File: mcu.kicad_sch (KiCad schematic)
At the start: 29 parts, among them U1 NRF52840-QIAA-R, Y1 32.768 kHz, Y2 32 MHz

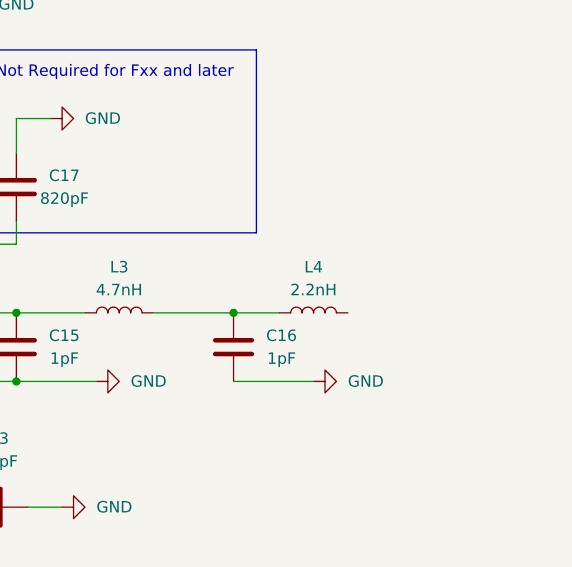
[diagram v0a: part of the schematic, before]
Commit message: Added 0 Ohm resistor before antenna for later VNA tuning
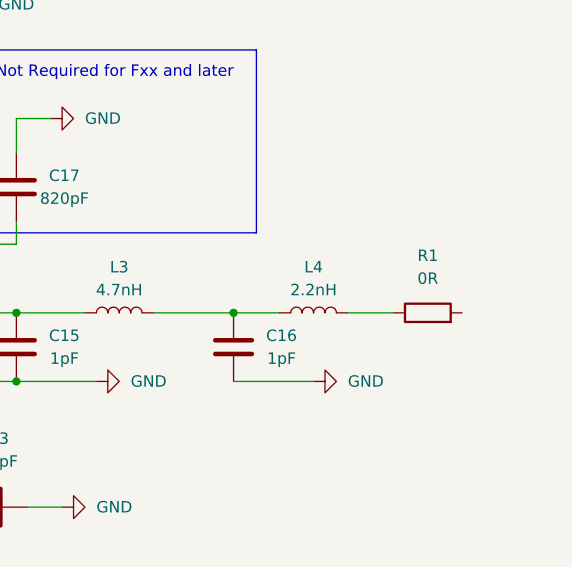
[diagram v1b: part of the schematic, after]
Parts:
- added R1: 0R, symbol Device:R
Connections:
- net at L4.2: now also R1.1
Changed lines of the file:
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@@
+	(wire
+		(pts
+			(xy 255.27 120.65) (xy 260.35 120.65)
+		)
+		(stroke
+			(width 0)
+			(type default)
+		)
+	)
 	(wire
 		(pts
@@
 					(unit 1)
 				)
+			)
+		)
+	)
+	(symbol
+		(lib_id "Device:R")
+		(at 264.16 120.65 90)
+		(unit 1)
+		(exclude_from_sim no)
+		(in_bom yes)
+		(on_board yes)
+		(dnp no)
+		(fields_autoplaced yes)
+		(property "Reference" "R1"
+			(at 264.16 114.3 90)
+			(effects
+				(font
+					(size 1.27 1.27)
+				)
+			)
+		)
+		(property "Value" "0R"
+			(at 264.16 116.84 90)
+			(effects
+				(font
+					(size 1.27 1.27)
+				)
+			)
+		)
+		(property "Footprint" ""
+			(at 264.16 122.428 90)
+			(effects
+				(font
+					(size 1.27 1.27)
+				)
+				(hide yes)
+			)
+		)
+		(property "Datasheet" "~"
+			(at 264.16 120.65 0)
+			(effects
+				(font
+					(size 1.27 1.27)
+				)
+				(hide yes)
+			)
+		)
+		(property "Description" "Resistor"
+			(at 264.16 120.65 0)
+			(effects
+				(font
+					(size 1.27 1.27)
+				)
+				(hide yes)
+			)
+		)
+		(pin "2"
+		)
+		(pin "1"
+		)
+		(instances
+			(project ""
+				(path "/5d65a0d4-45a3-4af0-996a-c0381d04499a/f42a8a8a-4a34-440a-8e58-9c442fe0d23e"
+					(reference "R1")
+					(unit 1)
+				)

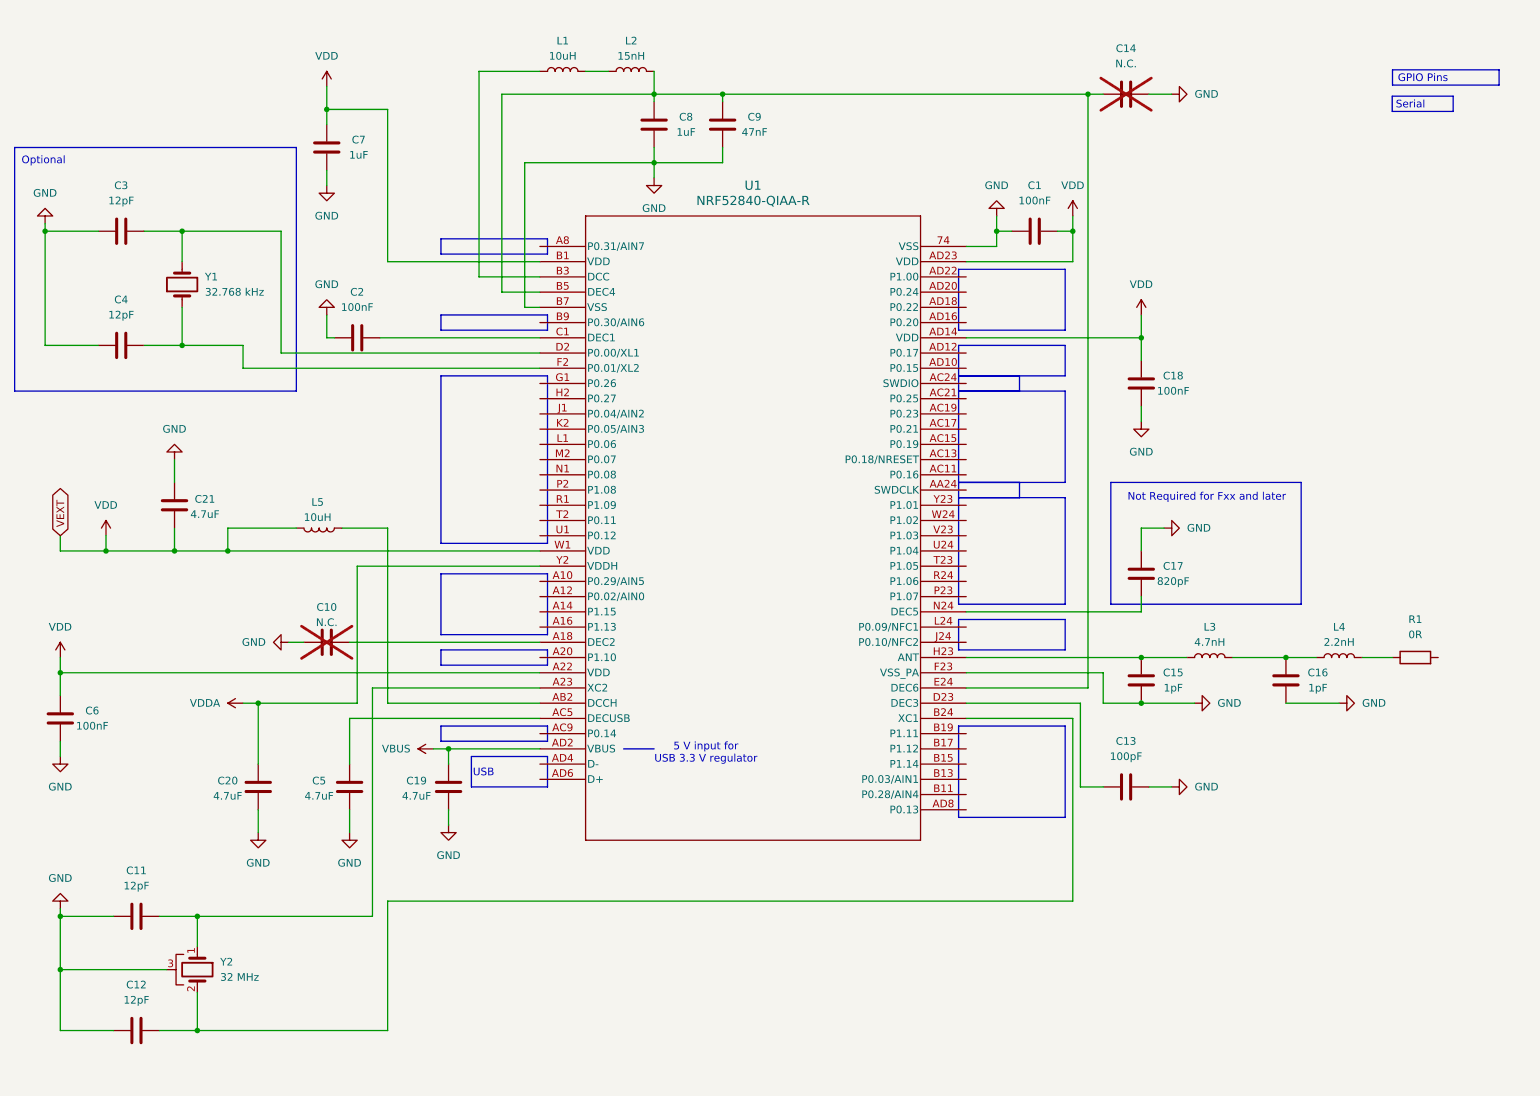
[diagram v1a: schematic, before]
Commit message: Added proper Labels
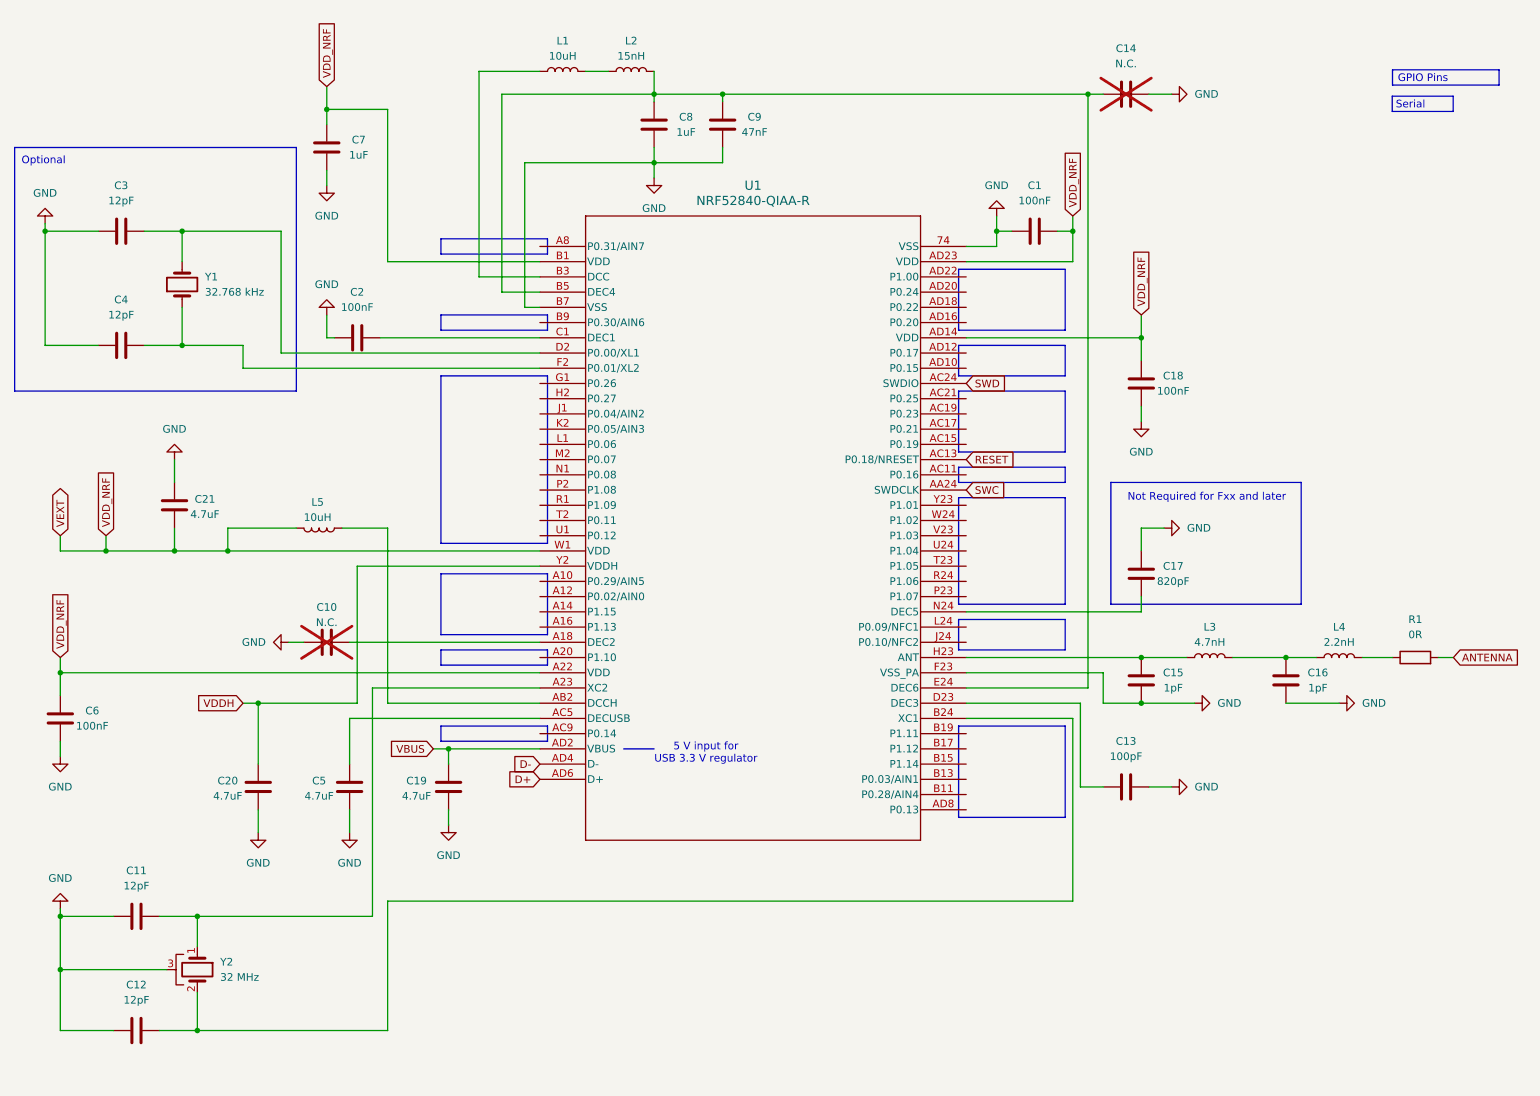
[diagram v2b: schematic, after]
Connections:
- net ANTENNA: now reaches R1.2
- net SWC: now reaches U1.AA24 (SWDCLK)
- net RESET: now reaches U1.AC13 (P0.18/NRESET)
- net SWD: now reaches U1.AC24 (SWDIO)
- net D-: now reaches U1.AD4 (D-)
- net D+: now reaches U1.AD6 (D+)
- net VDD renamed VDD_NRF
- net VDDA renamed VDDH
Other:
- note removed: "USB"

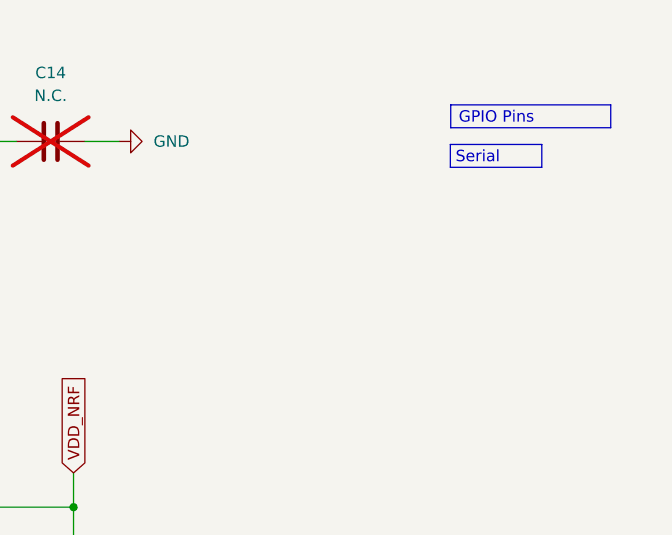
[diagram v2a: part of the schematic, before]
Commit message: Added charging schematic
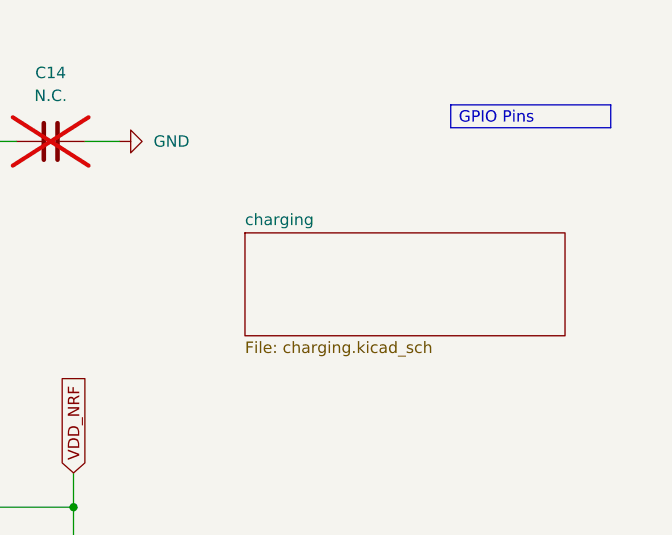
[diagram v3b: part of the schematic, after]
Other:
- added sheet charging (charging.kicad_sch)
- note removed: "Serial"
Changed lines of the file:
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@@
 	)
 	(rectangle
-		(start 260.3084 27.0049)
-		(end 270.4684 29.5449)
-		(stroke
-			(width 0)
-			(type default)
-		)
-		(fill
-			(type none)
-		)
-	)
-	(rectangle
 		(start 187.96 114.3)
 		(end 205.74 119.38)
@@
 		)
 	)
-	(text "Serial"
-		(exclude_from_sim no)
-		(at 263.3564 28.5289 0)
-		(effects
-			(font
-				(size 1.27 1.27)
-			)
-		)
-	)
 	(junction
 		(at 71.12 128.27)
@@
 			)
 		)
-		(property "Description" ""
+		(property "Description" "https://www.digikey.de/de/products/detail/nordic-semiconductor-asa/NRF52840-QIAA-F-R/15929794"
 			(at 118.11 52.07 0)
 			(effects
@@
 				)
 			)
+		)
+	)
+	(sheet
+		(at 237.49 36.83)
+		(size 35.56 11.43)
+		(exclude_from_sim no)
+		(in_bom yes)
+		(on_board yes)
+		(dnp no)
+		(fields_autoplaced yes)
+		(stroke
+			(width 0.1524)
+			(type solid)
+		)
+		(fill
+			(color 0 0 0 0.0000)
+		)
+		(property "Sheetname" "charging"
+			(at 237.49 36.1184 0)
+			(effects
+				(font
+					(size 1.27 1.27)
+				)
+				(justify left bottom)
+			)
+		)
+		(property "Sheetfile" "charging.kicad_sch"
+			(at 237.49 48.8446 0)
+			(effects
+				(font
+					(size 1.27 1.27)
+				)
+				(justify left top)
+			)
+		)
+		(instances
+			(project "Slim Keyboard"
+				(path "/5d65a0d4-45a3-4af0-996a-c0381d04499a/f42a8a8a-4a34-440a-8e58-9c442fe0d23e"
+					(page "5")
+				)
+			)

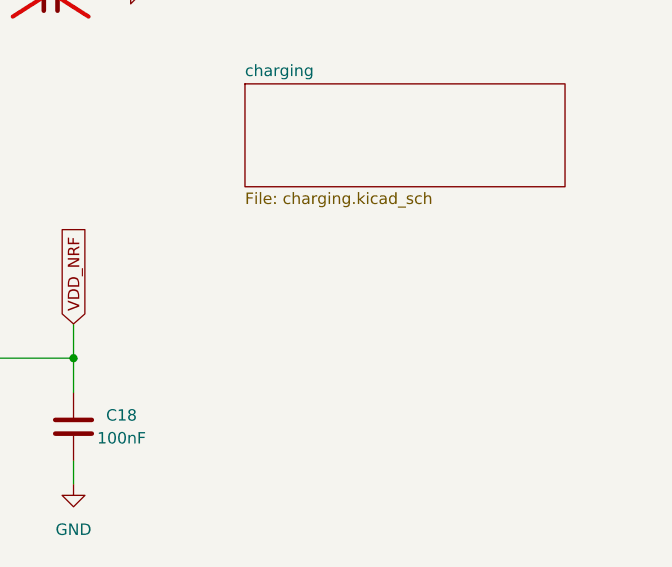
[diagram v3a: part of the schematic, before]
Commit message: Added external VCC schematic
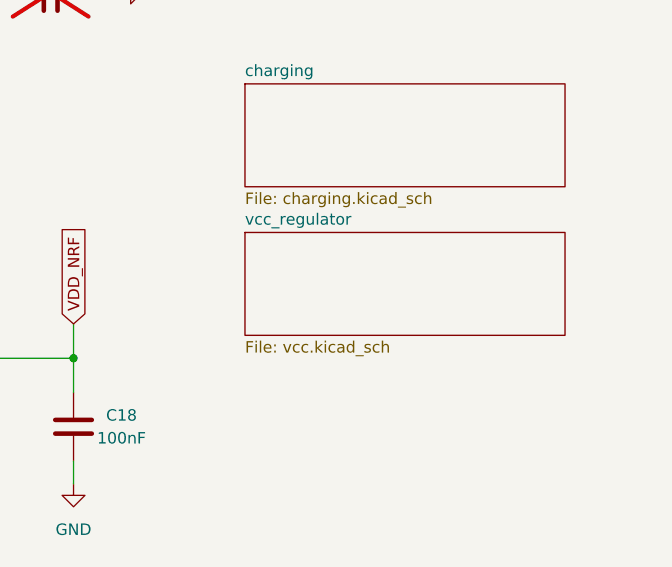
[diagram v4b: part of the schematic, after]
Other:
- added sheet vcc_regulator (vcc.kicad_sch)
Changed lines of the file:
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@@
+	)
+	(sheet
+		(at 237.49 53.34)
+		(size 35.56 11.43)
+		(exclude_from_sim no)
+		(in_bom yes)
+		(on_board yes)
+		(dnp no)
+		(fields_autoplaced yes)
+		(stroke
+			(width 0.1524)
+			(type solid)
+		)
+		(fill
+			(color 0 0 0 0.0000)
+		)
+		(property "Sheetname" "vcc_regulator"
+			(at 237.49 52.6284 0)
+			(effects
+				(font
+					(size 1.27 1.27)
+				)
+				(justify left bottom)
+			)
+		)
+		(property "Sheetfile" "vcc.kicad_sch"
+			(at 237.49 65.3546 0)
+			(effects
+				(font
+					(size 1.27 1.27)
+				)
+				(justify left top)
+			)
+		)
+		(instances
+			(project "Slim Keyboard"
+				(path "/5d65a0d4-45a3-4af0-996a-c0381d04499a/f42a8a8a-4a34-440a-8e58-9c442fe0d23e"
+					(page "6")
+				)
+			)
+		)
 	)
 	(sheet

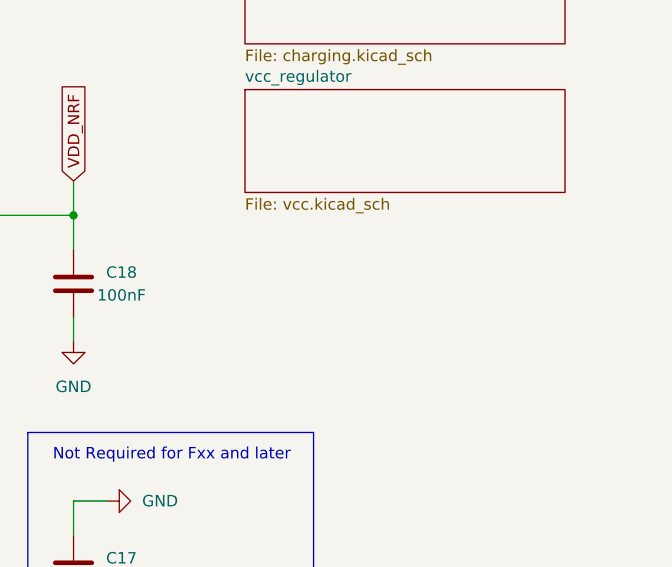
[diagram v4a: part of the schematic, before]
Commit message: Added USB connection
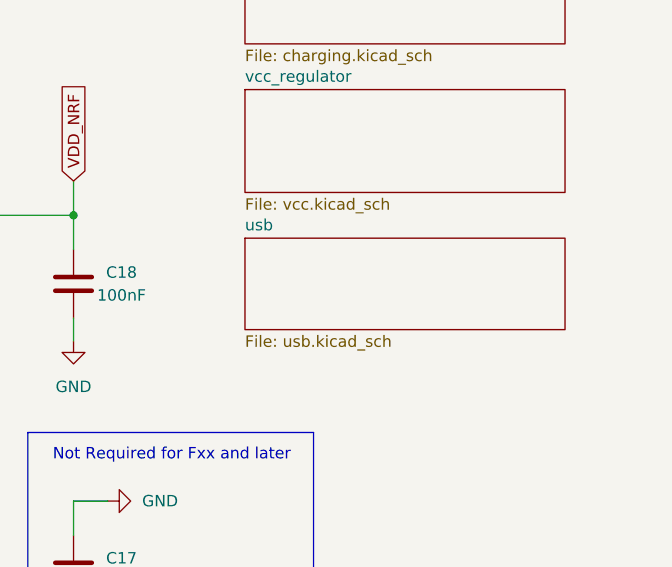
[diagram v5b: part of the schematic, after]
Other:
- added sheet usb (usb.kicad_sch)
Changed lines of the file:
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@@
 	(wire
 		(pts
+			(xy 218.44 78.74) (xy 218.44 81.28)
+		)
+		(stroke
+			(width 0)
+			(type default)
+		)
+	)
+	(wire
+		(pts
 			(xy 77.47 99.06) (xy 66.04 99.06)
 		)
@@
 	(wire
 		(pts
-			(xy 218.44 78.74) (xy 218.44 81.28)
-		)
-		(stroke
-			(width 0)
-			(type default)
-		)
-	)
-	(wire
-		(pts
 			(xy 118.11 54.61) (xy 92.71 54.61)
 		)
@@
 				)
 			)
+		)
+	)
+	(sheet
+		(at 237.49 69.85)
+		(size 35.56 10.16)
+		(exclude_from_sim no)
+		(in_bom yes)
+		(on_board yes)
+		(dnp no)
+		(fields_autoplaced yes)
+		(stroke
+			(width 0.1524)
+			(type solid)
+		)
+		(fill
+			(color 0 0 0 0.0000)
+		)
+		(property "Sheetname" "usb"
+			(at 237.49 69.1384 0)
+			(effects
+				(font
+					(size 1.27 1.27)
+				)
+				(justify left bottom)
+			)
+		)
+		(property "Sheetfile" "usb.kicad_sch"
+			(at 237.49 80.5946 0)
+			(effects
+				(font
+					(size 1.27 1.27)
+				)
+				(justify left top)
+			)
+		)
+		(instances
+			(project "Slim Keyboard"
+				(path "/5d65a0d4-45a3-4af0-996a-c0381d04499a/f42a8a8a-4a34-440a-8e58-9c442fe0d23e"
+					(page "7")
+				)
+			)

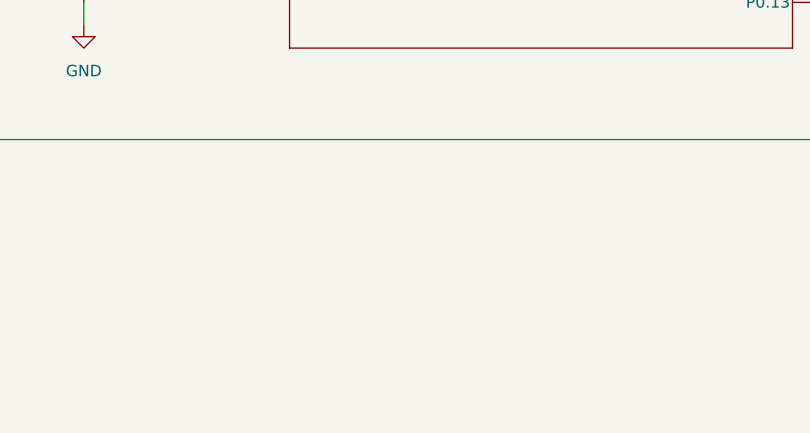
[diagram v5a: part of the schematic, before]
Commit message: Update footprints
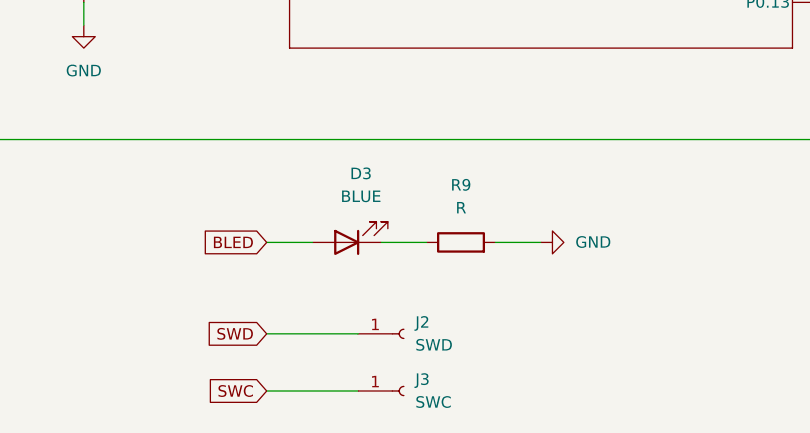
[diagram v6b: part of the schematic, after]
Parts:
- added D3: BLUE, symbol Device:LED
- added J2: SWD, TestPoint:TestPoint_Pad_2.5x2.5mm, symbol Connector:Conn_01x01_Socket
- added J3: SWC, TestPoint:TestPoint_Pad_2.5x2.5mm, symbol Connector:Conn_01x01_Socket
- added R9: R, symbol Device:R
- C1, C10, C11, C12, C13, C14, C15, C16, C17, C18, C2, C3, C4, C6, C9: footprint (none) -> Capacitor_SMD:C_0402_1005Metric
- C19, C20, C21, C5, C7, C8: footprint (none) -> Capacitor_SMD:C_0603_1608Metric
- L1, L5: footprint (none) -> Inductor_SMD:L_0603_1608Metric
- L2, L3, L4: footprint (none) -> Inductor_SMD:L_0402_1005Metric
- Y1: footprint (none) -> Crystal:Crystal_SMD_3215-2Pin_3.2x1.5mm
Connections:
- net GND: now also R9.2
- net SWC: now also J3.1 (Pin_1)
- net SWD: now also J2.1 (Pin_1)
- new net: D3.1 (K), R9.1
- new net BLED: D3.2 (A)
